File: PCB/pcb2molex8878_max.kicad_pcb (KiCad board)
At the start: 2 copper layers, 16.7 x 39.8 mm, 2 parts

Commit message: fix pocket dims to account for fitment clearance
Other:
- board text added: "after drill & mill, all inside corners"
- board text added: "mill radius"
- board text added: "partial mill radius fillet will be left"
- board text removed: "partial mill radius fillet"
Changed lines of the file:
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@@
   (general
     (thickness 1.6)
-    (drawings 41)
+    (drawings 49)
     (tracks 0)
     (zones 0)
@@
     (uvia_min_size 0.508)
     (uvia_min_drill 0.1524)
-    (edge_width 0.0254)
+    (edge_width 0.02)
     (segment_width 0.2032)
     (pcb_text_width 0.254)
@@
       (solder_mask_margin -0.19))
   )
+  (dimension 2 (width 0.0127) (layer Dwgs.User)
+    (gr_text 2.00 (at 150.5684 77.1044) (layer Dwgs.User)
+      (effects (font (size 0.4572 0.4572) (thickness 0.0127)) (justify right))
+    )
+    (feature1 (pts (xy 151.5684 79.287) (xy 151.5684 77.000579)))
+    (feature2 (pts (xy 149.5684 79.287) (xy 149.5684 77.000579)))
+    (crossbar (pts (xy 149.5684 77.587) (xy 151.5684 77.587)))
+    (arrow1a (pts (xy 151.5684 77.587) (xy 150.441896 78.173421)))
+    (arrow1b (pts (xy 151.5684 77.587) (xy 150.441896 77.000579)))
+    (arrow2a (pts (xy 149.5684 77.587) (xy 150.694904 78.173421)))
+    (arrow2b (pts (xy 149.5684 77.587) (xy 150.694904 77.000579)))
+  )
+  (dimension 2 (width 0.0127) (layer Dwgs.User)
+    (gr_text 2.00 (at 152.5684 82.1196) (layer Dwgs.User)
+      (effects (font (size 0.4572 0.4572) (thickness 0.0127)) (justify right))
+    )
+    (feature1 (pts (xy 153.5684 80.087) (xy 153.5684 82.223421)))
+    (feature2 (pts (xy 151.5684 80.087) (xy 151.5684 82.223421)))
+    (crossbar (pts (xy 151.5684 81.637) (xy 153.5684 81.637)))
+    (arrow1a (pts (xy 153.5684 81.637) (xy 152.441896 82.223421)))
+    (arrow1b (pts (xy 153.5684 81.637) (xy 152.441896 81.050579)))
+    (arrow2a (pts (xy 151.5684 81.637) (xy 152.694904 82.223421)))
+    (arrow2b (pts (xy 151.5684 81.637) (xy 152.694904 81.050579)))
+  )
+  (gr_arc (start 152.428401 79.224911) (end 151.568402 79.28491) (angle -86.0090869) (layer Dwgs.User) (width 0.0127))
+  (gr_arc (start 148.7084 79.227) (end 148.7084 80.087) (angle -86.0090869) (layer Dwgs.User) (width 0.0127))
+  (gr_arc (start 149.076315 119.146855) (end 149.076315 118.286855) (angle -86.0090869) (layer Dwgs.User) (width 0.0127))
+  (gr_arc (start 145.358399 119.149089) (end 146.218398 119.08909) (angle -86.0090869) (layer Dwgs.User) (width 0.0127))
+  (gr_line (start 141.4184 118.487) (end 141.6684 118.487) (layer Dwgs.User) (width 0.02))
+  (gr_line (start 141.4184 118.487) (end 141.4184 118.737) (layer Dwgs.User) (width 0.02))
+  (gr_line (start 141.4184 118.487) (end 142.3184 119.387) (layer Dwgs.User) (width 0.02))
+  (gr_text "mill radius" (at 143.0684 115.587) (layer Dwgs.User)
+    (effects (font (size 0.4572 0.4572) (thickness 0.0127)))
+  )
+  (gr_text "after drill & mill, all inside corners" (at 144.0184 119.887) (layer Dwgs.User)
+    (effects (font (size 0.2 0.2) (thickness 0.0127)))
+  )
   (gr_line (start 149.5684 80.087) (end 142.8684 80.087) (layer Edge.Cuts) (width 0.0254))
   (gr_line (start 149.5684 79.287) (end 149.5684 80.087) (layer Edge.Cuts) (width 0.0254))
@@
   (gr_line (start 138.8684 119.087) (end 140.8684 119.087) (layer Edge.Cuts) (width 0.0254))
   (gr_line (start 140.8684 119.087) (end 140.8684 118.287) (layer Edge.Cuts) (width 0.0254))
-  (gr_line (start 141.2184 118.237) (end 141.4184 118.037) (layer Dwgs.User) (width 0.0127))
-  (gr_line (start 141.2184 118.237) (end 141.0184 118.037) (layer Dwgs.User) (width 0.0127))
-  (gr_text "partial mill radius fillet" (at 144.3184 117.287) (layer Dwgs.User)
-    (effects (font (size 0.4572 0.4572) (thickness 0.0127)))
-  )
-  (gr_line (start 141.2184 118.237) (end 141.2184 117.687) (layer Dwgs.User) (width 0.0127))
+  (gr_text "partial mill radius fillet will be left" (at 144.0184 119.537) (layer Dwgs.User)
+    (effects (font (size 0.2 0.2) (thickness 0.0127)))
+  )
   (gr_poly (pts (xy 140.8684 118.286575) (xy 141.7284 118.286855) (xy 141.59738 118.29796) (xy 141.52118 118.3132) (xy 141.47546 118.3259) (xy 141.41704 118.34622) (xy 141.37386 118.364) (xy 141.3383 118.38178) (xy 141.30782 118.39702) (xy 141.2875 118.40972) (xy 141.27226 118.41988) (xy 141.23924 118.4402) (xy 141.20876 118.46306) (xy 141.183724 118.481284) (xy 141.15796 118.4402) (xy 141.13256 118.40718) (xy 141.10208 118.3767) (xy 141.0716 118.3513) (xy 141.02842 118.3259) (xy 140.9954 118.31066) (xy 140.96492 118.3005) (xy 140.92936 118.29288) (xy 140.90904 118.29034)) (layer Dwgs.User) (width 0.001))
-  (dimension 0.860058 (width 0.0127) (layer Dwgs.User)
-    (gr_text "   0.86 mill radius" (at 141.314303 120.519679 0.7) (layer Dwgs.User)
+  (dimension 0.86 (width 0.0127) (layer Dwgs.User)
+    (gr_text 0.86 (at 141.298058 116.254472) (layer Dwgs.User)
       (effects (font (size 0.4572 0.4572) (thickness 0.0127)) (justify left))
     )
-    (feature1 (pts (xy 141.7284 119.147) (xy 141.74551 120.618493)))
-    (feature2 (pts (xy 140.8684 119.157) (xy 140.88551 120.628493)))
-    (crossbar (pts (xy 140.878692 120.042112) (xy 141.738692 120.032112)))
-    (arrow1a (pts (xy 141.738692 120.032112) (xy 140.619083 120.631591)))
-    (arrow1b (pts (xy 141.738692 120.032112) (xy 140.605446 119.458829)))
-    (arrow2a (pts (xy 140.878692 120.042112) (xy 142.011938 120.615395)))
-    (arrow2b (pts (xy 140.878692 120.042112) (xy 141.998301 119.442633)))
+    (feature1 (pts (xy 141.7284 118.286855) (xy 141.72804 116.150579)))
+    (feature2 (pts (xy 140.8684 118.287) (xy 140.86804 116.150724)))
+    (crossbar (pts (xy 140.868139 116.737145) (xy 141.728139 116.737)))
+    (arrow1a (pts (xy 141.728139 116.737) (xy 140.601734 117.323611)))
+    (arrow1b (pts (xy 141.728139 116.737) (xy 140.601536 116.150769)))
+    (arrow2a (pts (xy 140.868139 116.737145) (xy 141.994742 117.323376)))
+    (arrow2b (pts (xy 140.868139 116.737145) (xy 141.994544 116.150534)))
   )
   (gr_arc (start 141.7284 119.147) (end 141.7284 118.286855) (angle -39.28940686) (layer Dwgs.User) (width 0.0127))
@@
     (arrow2b (pts (xy 138.8684 73.237) (xy 139.994904 72.650579)))
   )
-  (dimension 0.7 (width 0.0127) (layer Dwgs.User)
-    (gr_text "   0.70" (at 142.8684 81.9696) (layer Dwgs.User)
+  (dimension 0.8 (width 0.0127) (layer Dwgs.User)
+    (gr_text 0.80 (at 142.8684 81.7196) (layer Dwgs.User)
       (effects (font (size 0.4572 0.4572) (thickness 0.0127)) (justify left))
     )
-    (feature1 (pts (xy 143.2184 79.737) (xy 143.2184 82.073421)))
-    (feature2 (pts (xy 142.5184 79.737) (xy 142.5184 82.073421)))
-    (crossbar (pts (xy 142.5184 81.487) (xy 143.2184 81.487)))
-    (arrow1a (pts (xy 143.2184 81.487) (xy 142.091896 82.073421)))
-    (arrow1b (pts (xy 143.2184 81.487) (xy 142.091896 80.900579)))
-    (arrow2a (pts (xy 142.5184 81.487) (xy 143.644904 82.073421)))
-    (arrow2b (pts (xy 142.5184 81.487) (xy 143.644904 80.900579)))
+    (feature1 (pts (xy 143.2684 79.737) (xy 143.2684 81.823421)))
+    (feature2 (pts (xy 142.4684 79.737) (xy 142.4684 81.823421)))
+    (crossbar (pts (xy 142.4684 81.237) (xy 143.2684 81.237)))
+    (arrow1a (pts (xy 143.2684 81.237) (xy 142.141896 81.823421)))
+    (arrow1b (pts (xy 143.2684 81.237) (xy 142.141896 80.650579)))
+    (arrow2a (pts (xy 142.4684 81.237) (xy 143.594904 81.823421)))
+    (arrow2b (pts (xy 142.4684 81.237) (xy 143.594904 80.650579)))
   )
   (dimension 2 (width 0.0127) (layer Dwgs.User)
-    (gr_text "2.00    " (at 154.5684 76.4544) (layer Dwgs.User)
+    (gr_text 2.00 (at 154.5684 76.4544) (layer Dwgs.User)
       (effects (font (size 0.4572 0.4572) (thickness 0.0127)) (justify right))
     )

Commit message: show retainer wedges on pcb drawings. add daughterboard in carrier model.
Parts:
- gave numbers to parts that had none: 2
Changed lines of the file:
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@@
     (diff_pair_gap 0.254)
-  )
-  (module 000_LOCAL:pcb2molex8878_max (layer Top)
-    (at 147.2184 99.187)
-    (descr "Castellated edge contacts to fit Molex 8878 Socket")
-    (solder_mask_margin -0.28)
-    (fp_text reference J? (at -0.9906 -0.9906 -90) (layer Dwgs.User) hide
-      (effects (font (size 1.2065 1.2065) (thickness 0.127)) (justify left bottom))
-    )
-    (fp_text value pcb2molex8878_max (at 2.23 -9.45 -90) (layer F.Fab) hide
-      (effects (font (size 1.2065 1.2065) (thickness 0.1016)) (justify left bottom))
-    )
-    (fp_line (start 2.35 -19.1) (end -4.35 -19.1) (layer Eco2.User) (width 0.01))
-    (fp_line (start 2.35 -19.9) (end 2.35 -19.1) (layer Eco2.User) (width 0.01))
-    (fp_line (start 4.35 -19.9) (end 2.35 -19.9) (layer Eco2.User) (width 0.01))
-    (fp_line (start 4.35 -19.1) (end 4.35 -19.9) (layer Eco2.User) (width 0.01))
-    (fp_line (start 6.35 -19.1) (end 4.35 -19.1) (layer Eco2.User) (width 0.01))
-    (fp_line (start 6.35 19.1) (end 1 19.1) (layer Eco2.User) (width 0.01))
-    (fp_line (start -1 19.1) (end -1 19.9) (layer Eco2.User) (width 0.01))
-    (fp_line (start -6.35 19.1) (end -1 19.1) (layer Eco2.User) (width 0.01))
-    (fp_line (start 1 19.1) (end 1 19.9) (layer Eco2.User) (width 0.01))
-    (fp_line (start -1 19.9) (end 1 19.9) (layer Eco2.User) (width 0.01))
-    (fp_line (start -8.35 19.9) (end -6.35 19.9) (layer Eco2.User) (width 0.01))
-    (fp_line (start 8.35 19.9) (end 6.35 19.9) (layer Eco2.User) (width 0.01))
-    (fp_line (start 8.35 -19.9) (end 6.35 -19.9) (layer Eco2.User) (width 0.01))
-    (fp_line (start -8.35 -19.9) (end -4.35 -19.9) (layer Eco2.User) (width 0.01))
-    (fp_line (start -8.35 -19.1) (end 8.35 19.1) (layer Dwgs.User) (width 0.01))
-    (fp_line (start -8.35 19.1) (end 8.35 -19.1) (layer Dwgs.User) (width 0.01))
-    (fp_text user "Eco2.User is Edge.Cuts for use with \"pcb2molex8878_max\" carrier." (at -0.18 13.04) (layer Eco2.User)
-      (effects (font (size 0.2 0.2) (thickness 0.01)))
-    )
-    (fp_line (start -8.35 -19.9) (end -8.35 19.9) (layer Eco2.User) (width 0.01))
-    (fp_line (start 8.35 19.9) (end 8.35 -19.9) (layer Eco2.User) (width 0.01))
-    (fp_line (start -6.35 19.1) (end -6.35 19.9) (layer Eco2.User) (width 0.01))
-    (fp_line (start 6.35 19.9) (end 6.35 19.1) (layer Eco2.User) (width 0.01))
-    (fp_line (start 6.35 -19.1) (end 6.35 -19.9) (layer Eco2.User) (width 0.01))
-    (fp_line (start -4.35 -19.9) (end -4.35 -19.1) (layer Eco2.User) (width 0.01))
-    (pad "" np_thru_hole circle (at -1 19.5) (size 0.8 0.8) (drill 0.8) (layers *.Cu))
-    (pad "" np_thru_hole circle (at 1 19.5) (size 0.8 0.8) (drill 0.8) (layers *.Cu))
-    (pad "" np_thru_hole circle (at 4.35 -19.5) (size 0.8 0.8) (drill 0.8) (layers *.Cu))
-    (pad "" np_thru_hole circle (at 2.35 -19.5) (size 0.8 0.8) (drill 0.8) (layers *.Cu))
-    (pad "" np_thru_hole circle (at 8.35 19.5) (size 0.8 0.8) (drill 0.8) (layers *.Cu))
-    (pad "" np_thru_hole circle (at -8.35 19.5) (size 0.8 0.8) (drill 0.8) (layers *.Cu))
-    (pad "" np_thru_hole circle (at 8.35 -19.5) (size 0.8 0.8) (drill 0.8) (layers *.Cu))
-    (pad "" np_thru_hole circle (at -8.35 -19.5) (size 0.8 0.8) (drill 0.8) (layers *.Cu))
-    (pad "" np_thru_hole circle (at 6.35 19.5) (size 0.8 0.8) (drill 0.8) (layers *.Cu))
-    (pad "" np_thru_hole circle (at -6.35 19.5) (size 0.8 0.8) (drill 0.8) (layers *.Cu))
-    (pad "" np_thru_hole circle (at 6.35 -19.5) (size 0.8 0.8) (drill 0.8) (layers *.Cu))
-    (pad "" np_thru_hole circle (at -4.35 -19.5) (size 0.8 0.8) (drill 0.8) (layers *.Cu))
-    (model ${KIPRJMOD}/000_LOCAL.pretty/3d/pcb2molex8878_max.step
-      (offset (xyz 0 0 -0.4))
-      (scale (xyz 1 1 1))
-      (rotate (xyz 0 0 90))
-    )
   )
   (module 000_LOCAL:pcb2molex8878 locked (layer Top)
@@
     (descr "Castellated edge contacts to fit Molex 8878 Socket")
     (solder_mask_margin -0.28)
-    (fp_text reference J? (at -0.9906 -0.9906 -90) (layer Dwgs.User) hide
+    (fp_text reference contacts1 (at -0.9906 -0.9906 -90) (layer Dwgs.User) hide
       (effects (font (size 1.2065 1.2065) (thickness 0.127)) (justify left bottom))
     )
@@
       (solder_mask_margin -0.19))
   )
+  (module 000_LOCAL:pcb2molex8878_max (layer Top)
+    (at 147.2184 99.187)
+    (descr "Castellated edge contacts to fit Molex 8878 Socket")
+    (solder_mask_margin -0.28)
+    (fp_text reference carrier1 (at -0.9906 -0.9906 -90) (layer Dwgs.User) hide
+      (effects (font (size 1.2065 1.2065) (thickness 0.127)) (justify left bottom))
+    )
+    (fp_text value pcb2molex8878_max (at 2.23 -9.45 -90) (layer F.Fab) hide
+      (effects (font (size 1.2065 1.2065) (thickness 0.1016)) (justify left bottom))
+    )
+    (fp_line (start 2.35 -19.1) (end -4.35 -19.1) (layer Eco2.User) (width 0.01))
+    (fp_line (start 2.35 -19.9) (end 2.35 -19.1) (layer Eco2.User) (width 0.01))
+    (fp_line (start 4.35 -19.9) (end 2.35 -19.9) (layer Eco2.User) (width 0.01))
+    (fp_line (start 4.35 -19.1) (end 4.35 -19.9) (layer Eco2.User) (width 0.01))
+    (fp_line (start 6.35 -19.1) (end 4.35 -19.1) (layer Eco2.User) (width 0.01))
+    (fp_line (start 6.35 19.1) (end 1 19.1) (layer Eco2.User) (width 0.01))
+    (fp_line (start -1 19.1) (end -1 19.9) (layer Eco2.User) (width 0.01))
+    (fp_line (start -6.35 19.1) (end -1 19.1) (layer Eco2.User) (width 0.01))
+    (fp_line (start 1 19.1) (end 1 19.9) (layer Eco2.User) (width 0.01))
+    (fp_line (start -1 19.9) (end 1 19.9) (layer Eco2.User) (width 0.01))
+    (fp_line (start -8.35 19.9) (end -6.35 19.9) (layer Eco2.User) (width 0.01))
+    (fp_line (start 8.35 19.9) (end 6.35 19.9) (layer Eco2.User) (width 0.01))
+    (fp_line (start 8.35 -19.9) (end 6.35 -19.9) (layer Eco2.User) (width 0.01))
+    (fp_line (start -8.35 -19.9) (end -4.35 -19.9) (layer Eco2.User) (width 0.01))
+    (fp_line (start -8.35 -19.1) (end 8.35 19.1) (layer Dwgs.User) (width 0.01))
+    (fp_line (start -8.35 19.1) (end 8.35 -19.1) (layer Dwgs.User) (width 0.01))
+    (fp_text user "Eco2.User is Edge.Cuts for use with \"pcb2molex8878_max\" carrier." (at -0.18 13.04) (layer Eco2.User)
+      (effects (font (size 0.2 0.2) (thickness 0.01)))
+    )
+    (fp_line (start -8.35 -19.9) (end -8.35 19.9) (layer Eco2.User) (width 0.01))
+    (fp_line (start 8.35 19.9) (end 8.35 -19.9) (layer Eco2.User) (width 0.01))
+    (fp_line (start -6.35 19.1) (end -6.35 19.9) (layer Eco2.User) (width 0.01))
+    (fp_line (start 6.35 19.9) (end 6.35 19.1) (layer Eco2.User) (width 0.01))
+    (fp_line (start 6.35 -19.1) (end 6.35 -19.9) (layer Eco2.User) (width 0.01))
+    (fp_line (start -4.35 -19.9) (end -4.35 -19.1) (layer Eco2.User) (width 0.01))
+    (pad "" np_thru_hole circle (at -1 19.5) (size 0.8 0.8) (drill 0.8) (layers *.Cu))
+    (pad "" np_thru_hole circle (at 1 19.5) (size 0.8 0.8) (drill 0.8) (layers *.Cu))
+    (pad "" np_thru_hole circle (at 4.35 -19.5) (size 0.8 0.8) (drill 0.8) (layers *.Cu))
+    (pad "" np_thru_hole circle (at 2.35 -19.5) (size 0.8 0.8) (drill 0.8) (layers *.Cu))
+    (pad "" np_thru_hole circle (at 8.35 19.5) (size 0.8 0.8) (drill 0.8) (layers *.Cu))
+    (pad "" np_thru_hole circle (at -8.35 19.5) (size 0.8 0.8) (drill 0.8) (layers *.Cu))
+    (pad "" np_thru_hole circle (at 8.35 -19.5) (size 0.8 0.8) (drill 0.8) (layers *.Cu))
+    (pad "" np_thru_hole circle (at -8.35 -19.5) (size 0.8 0.8) (drill 0.8) (layers *.Cu))
+    (pad "" np_thru_hole circle (at 6.35 19.5) (size 0.8 0.8) (drill 0.8) (layers *.Cu))
+    (pad "" np_thru_hole circle (at -6.35 19.5) (size 0.8 0.8) (drill 0.8) (layers *.Cu))
+    (pad "" np_thru_hole circle (at 6.35 -19.5) (size 0.8 0.8) (drill 0.8) (layers *.Cu))
+    (pad "" np_thru_hole circle (at -4.35 -19.5) (size 0.8 0.8) (drill 0.8) (layers *.Cu))
+    (model ${KIPRJMOD}/000_LOCAL.pretty/3d/pcb2molex8878_max.step
+      (offset (xyz 0 0 -0.4))
+      (scale (xyz 1 1 1))
+      (rotate (xyz 0 0 90))
+    )
+  )
   (dimension 2 (width 0.0127) (layer Dwgs.User)

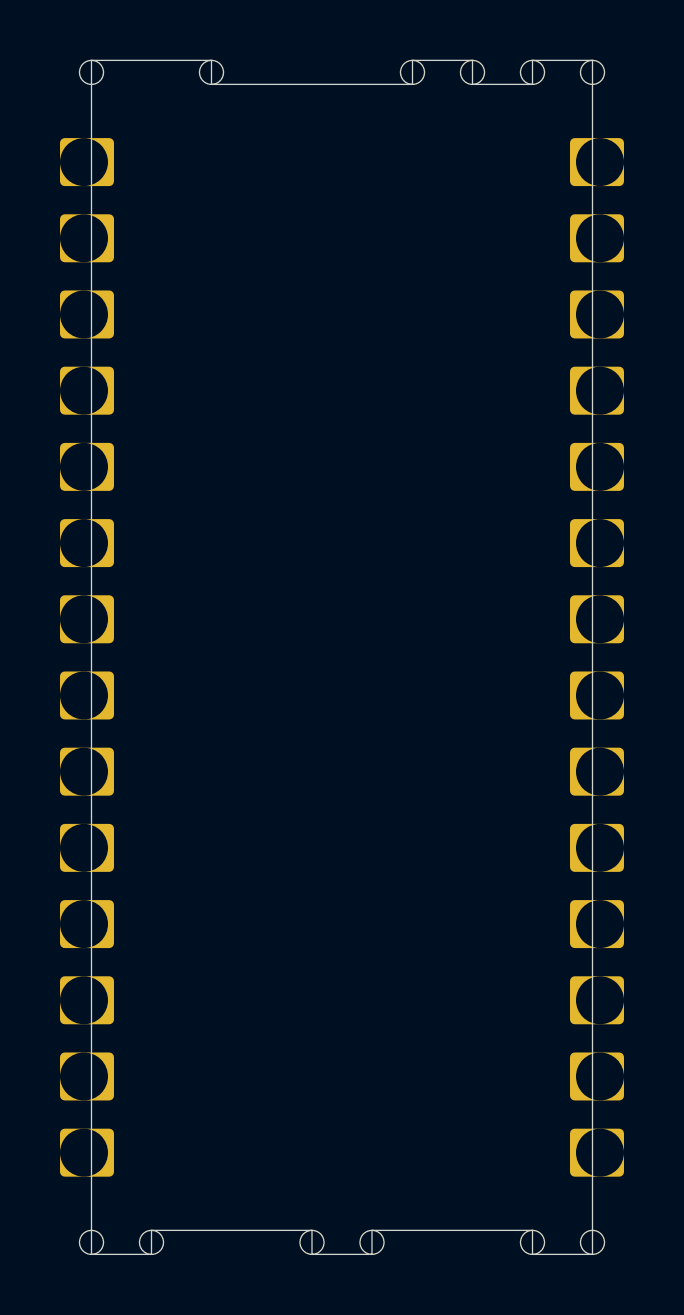
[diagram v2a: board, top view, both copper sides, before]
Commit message: reduce outside X & Y dims by 0.1mm all around
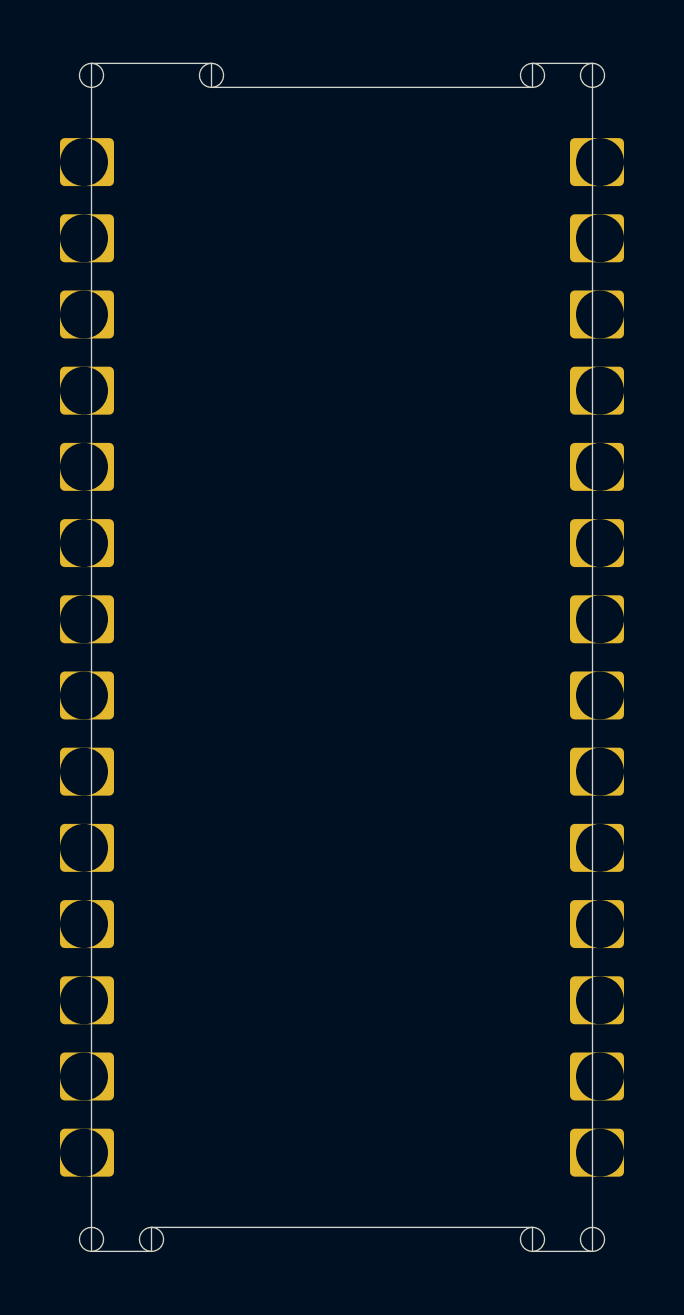
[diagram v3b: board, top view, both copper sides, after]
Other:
- board size 16.7 x 39.8 mm -> 16.7 x 39.6 mm
